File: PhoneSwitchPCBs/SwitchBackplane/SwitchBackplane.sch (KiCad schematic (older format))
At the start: 137 parts

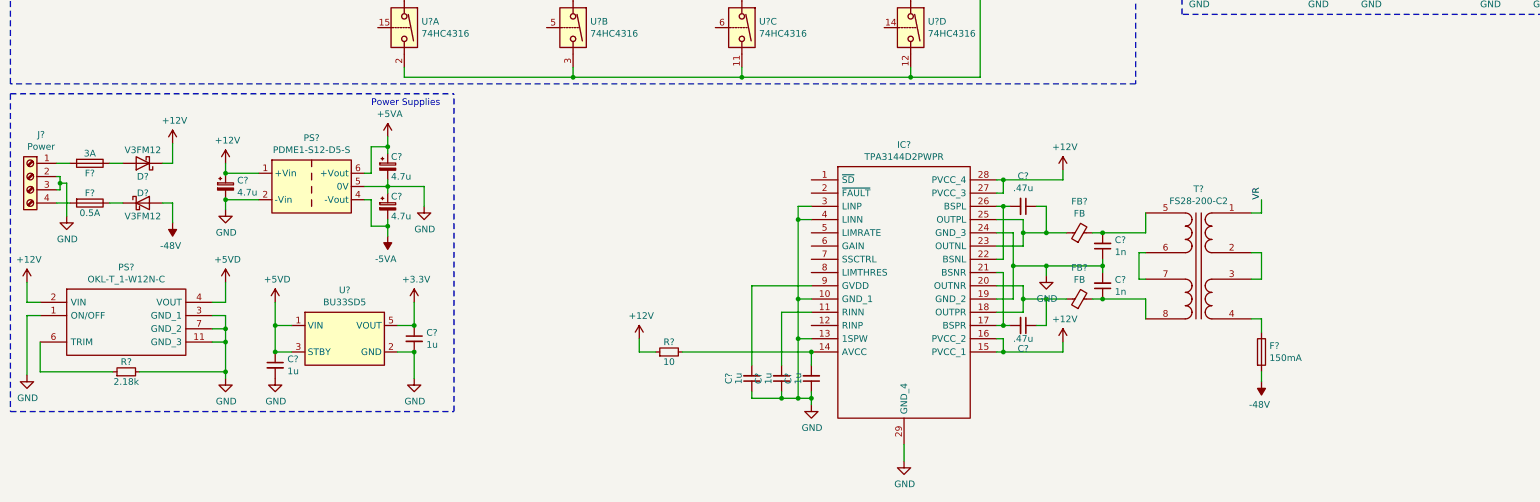
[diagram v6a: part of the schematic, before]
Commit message: Added ring generator oscillator spice sim and continued work on schematics
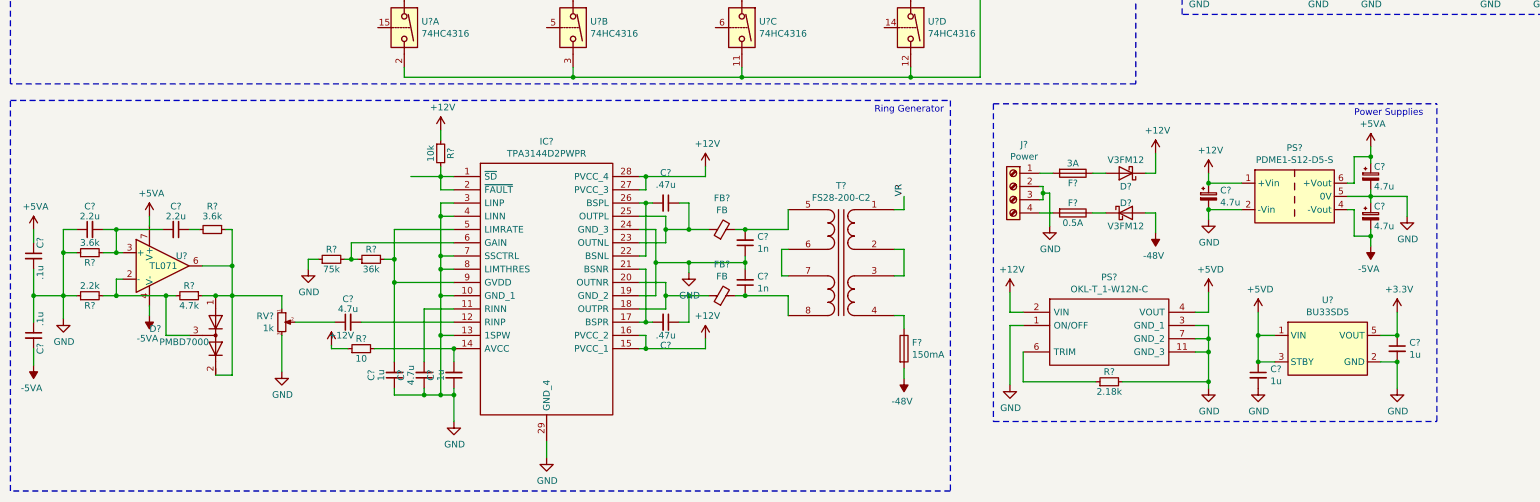
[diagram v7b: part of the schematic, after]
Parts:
- added C?: 4.7u, symbol Device:C_Small
- added C? (x2): 2.2u, symbol Device:C_Small
- added C? (x2): .1u, symbol Device:C_Small
- added D?: PMBD7000, Package_TO_SOT_SMD:SOT-23, symbol SwitchBackplaneParts:PMBD7000
- added R?: 36k, symbol Device:R_Small
- added R?: 75k, symbol Device:R_Small
- added R?: 10k, symbol Device:R_Small
- added R? (x2): 3.6k, symbol Device:R_Small
- added R?: 2.2k, symbol Device:R_Small
- added R?: 4.7k, symbol Device:R_Small
- added RV?: 1k, symbol Device:R_POT_Small
- added U?: TL071, symbol SwitchBackplaneParts:TL071
- C?: value 1u -> 4.7u
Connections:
- net +12V: now also R?.1
- net +5VA: now also C?.1, U?.7 (V+)
- net -5VA: now also C?.2, U?.4 (V-)
- net GND: now also IC?.7 (SSCTRL), IC?.8 (LIMTHRES), C?.1, C?.1, C?.2, R?.1, R?.1, R?.1, RV?.3
- net at IC?.1 (~SD): now also IC?.2 (~FAULT), R?.2
- net at IC?.12 (RINP): now also C?.2
- net at IC?.5 (LIMRATE): now also C?.2, IC?.9 (GVDD), R?.2
- net at IC?.6 (GAIN): now also R?.1, R?.2
- new net: C?.1, RV?.2
- new net: C?.2, C?.2, R?.2, U?.3 (+)
- new net: C?.1, R?.2
- new net: D?.1 (A1), D?.2 (K2), R?.1, R?.1, RV?.1, U?.6
- new net: D?.3 (K1A2), R?.2, R?.2, U?.2 (-)
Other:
- note added: "Ring Generator"
- moved on the sheet: C?, D?, F?, FB?, IC?, J?, PS?, R?, T?, U?

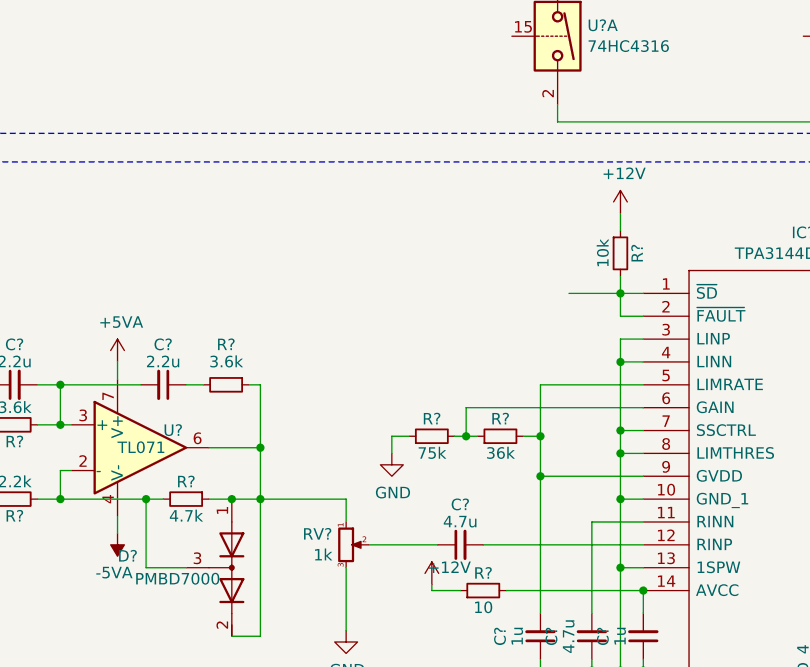
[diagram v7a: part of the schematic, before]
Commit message: Continue work on the backplane schematic and add Pi Pico footprint files
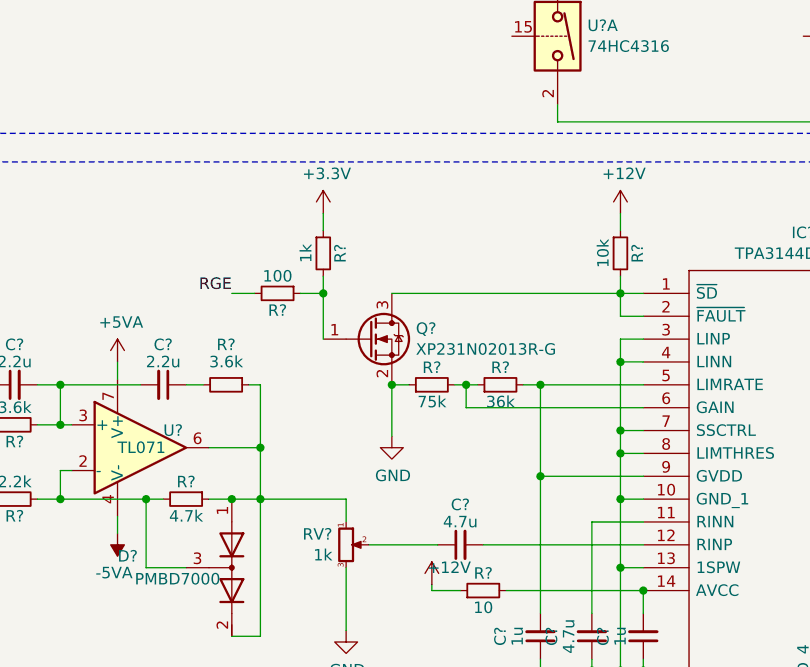
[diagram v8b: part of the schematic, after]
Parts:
- added Q?: XP231N02013R-G, Package_TO_SOT_SMD:SOT-323_SC-70_Handsoldering, symbol PhoneInterfaceParts:XP231N02013R-G
- added R?: 1k, symbol Device:R_Small
- added R?: 100, symbol Device:R_Small
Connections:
- net +3V3: now also R?.1
- net GND: now also Q?.2 (S)
- net at IC?.1 (~SD), IC?.2 (~FAULT), R?.2: now also Q?.3 (D)
- new net: Q?.1 (G), R?.1, R?.2
- new net RGE: R?.2
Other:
- moved on the sheet: R?
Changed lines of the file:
@@
 Wire Wire Line
 	4000 6975 3550 6975
-Wire Wire Line
-	3550 6975 3550 7200
 Connection ~ 3550 7375
-$Comp
-L power:GND #PWR?
-U 1 1 65949E95
-P 2900 7275
-F 0 "#PWR?" H 2900 7025 50  0001 C CNN
-F 1 "GND" H 2905 7102 50  0000 C CNN
-F 2 "" H 2900 7275 50  0001 C CNN
-F 3 "" H 2900 7275 50  0001 C CNN
-	1    2900 7275
-	1    0    0    -1
-$EndComp
-$Comp
-L Device:R_Small R?
-U 1 1 659D262B
-P 3375 7200
-F 0 "R?" V 3450 7200 50  0000 C CNN
-F 1 "36k" V 3300 7200 50  0000 C CNN
-F 2 "" H 3375 7200 50  0001 C CNN
-F 3 "~" H 3375 7200 50  0001 C CNN
-	1    3375 7200
-	0    -1   -1   0
-$EndComp
-$Comp
-L Device:R_Small R?
-U 1 1 659D3085
-P 3075 7200
-F 0 "R?" V 3150 7200 50  0000 C CNN
-F 1 "75k" V 3000 7200 50  0000 C CNN
-F 2 "" H 3075 7200 50  0001 C CNN
-F 3 "~" H 3075 7200 50  0001 C CNN
-	1    3075 7200
-	0    -1   -1   0
-$EndComp
-Wire Wire Line
-	3175 7200 3225 7200
-Wire Wire Line
-	2900 7200 2900 7275
-Connection ~ 3225 7200
-Wire Wire Line
-	3225 7200 3275 7200
 $Comp
 L Device:C_Small C?
@@
 	1    0    0    -1
 $EndComp
-Wire Wire Line
-	3675 6575 3900 6575
 Wire Wire Line
 	4000 6675 3900 6675
@@
 	825  7475 825  7675
 Wire Wire Line
-	3225 7075 3225 7200
-Wire Wire Line
-	3225 7075 4000 7075
-Wire Wire Line
 	4000 7175 3900 7175
 Connection ~ 3900 7175
@@
 Wire Wire Line
 	3900 7275 3900 7175
-Wire Wire Line
-	2900 7200 2975 7200
 $Comp
 L Device:R_POT_Small RV?
@@
 Wire Wire Line
 	3550 7975 3550 7375
-Wire Wire Line
-	3475 7200 3550 7200
-Connection ~ 3550 7200
-Wire Wire Line
-	3550 7200 3550 7375
 Wire Notes Line
 	650  6000 7750 6000
@@
 Text Notes 7700 6100 2    50   ~ 0
 Ring Generator
+$Comp
+L Device:R_Small R?
+U 1 1 694CBF4E
+P 2600 6400
+F 0 "R?" V 2675 6400 50  0000 C CNN
+F 1 "1k" V 2525 6400 50  0000 C CNN
+F 2 "" H 2600 6400 50  0001 C CNN
+F 3 "~" H 2600 6400 50  0001 C CNN
+	1    2600 6400
+	1    0    0    -1
+$EndComp
+$Comp
+L PhoneInterfaceParts:XP231N02013R-G Q?
+U 1 1 69235CAD
+P 2800 6775
+F 0 "Q?" H 3005 6821 50  0000 L CNN
+F 1 "XP231N02013R-G" H 3005 6730 50  0000 L CNN
+F 2 "Package_TO_SOT_SMD:SOT-323_SC-70_Handsoldering" H 3000 6700 50  0001 L CIN
+F 3 "https://www.torexsemi.com/file/XP231N02013R/XP231N02013R.pdf" H 2800 6775 50  0001 L CNN
+	1    2800 6775
+	1    0    0    -1
+$EndComp
+Wire Wire Line
+	3475 6975 3550 6975
+$Comp
+L Device:R_Small R?
+U 1 1 659D3085
+P 3075 6975
+F 0 "R?" V 3150 6975 50  0000 C CNN
+F 1 "75k" V 3000 6975 50  0000 C CNN
+F 2 "" H 3075 6975 50  0001 C CNN
+F 3 "~" H 3075 6975 50  0001 C CNN
+	1    3075 6975
+	0    -1   -1   0
+$EndComp
+$Comp
+L Device:R_Small R?
+U 1 1 659D262B
+P 3375 6975
+F 0 "R?" V 3450 6975 50  0000 C CNN
+F 1 "36k" V 3300 6975 50  0000 C CNN
+F 2 "" H 3375 6975 50  0001 C CNN
+F 3 "~" H 3375 6975 50  0001 C CNN
+	1    3375 6975
+	0    -1   -1   0
+$EndComp
+$Comp
+L power:GND #PWR?
+U 1 1 65949E95
+P 2900 7200
+F 0 "#PWR?" H 2900 6950 50  0001 C CNN
+F 1 "GND" H 2905 7027 50  0000 C CNN
+F 2 "" H 2900 7200 50  0001 C CNN
+F 3 "" H 2900 7200 50  0001 C CNN
+	1    2900 7200
+	1    0    0    -1
+$EndComp
+Wire Wire Line
+	2900 6575 3900 6575
+Wire Wire Line
+	2600 6775 2600 6575
+$Comp
+L power:+3.3V #PWR?
+U 1 1 698BA1FA
+P 2600 6225
+F 0 "#PWR?" H 2600 6075 50  0001 C CNN
+F 1 "+3.3V" H 2615 6398 50  0000 C CNN
+F 2 "" H 2600 6225 50  0001 C CNN
+F 3 "" H 2600 6225 50  0001 C CNN
+	1    2600 6225
+	1    0    0    -1
+$EndComp
+Wire Wire Line
+	2600 6225 2600 6300
+Connection ~ 3550 6975
+Wire Wire Line
+	3550 6975 3550 7375
+Wire Wire Line
+	3175 6975 3225 6975
+Wire Wire Line
+	2900 6975 2900 7200
+Wire Wire Line
+	2975 6975 2900 6975
+Connection ~ 2900 6975
+Wire Wire Line
+	3225 6975 3225 7075
+Wire Wire Line
+	3225 7075 4000 7075
+Connection ~ 3225 6975
+Wire Wire Line
+	3225 6975 3275 6975
+$Comp
+L Device:R_Small R?
+U 1 1 69C8FA00
+P 2400 6575
+F 0 "R?" V 2475 6575 50  0000 C CNN
+F 1 "100" V 2325 6575 50  0000 C CNN
+F 2 "" H 2400 6575 50  0001 C CNN
+F 3 "~" H 2400 6575 50  0001 C CNN
+	1    2400 6575
+	0    1    1    0
+$EndComp
+Wire Wire Line
+	2500 6575 2600 6575
+Connection ~ 2600 6575
+Wire Wire Line
+	2600 6575 2600 6500
+Wire Wire Line
+	2300 6575 2200 6575
+Text Label 2200 6575 2    50   ~ 0
+RGE
 $EndSCHEMATC
